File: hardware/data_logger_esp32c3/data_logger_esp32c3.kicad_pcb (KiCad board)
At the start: 4 copper layers, 43.3 x 32.3 mm, 74 parts, among them U1 ESP32-C3-MINI-1, U10 A03401A, U11 SX1509BIULTRT, U2 AZ1117IH-3.3TRG1, U4 LM321MF, U5 LM321MF, U6 LM321MF, U7 LM321MF, U8 LM321MF, U9 A03401A

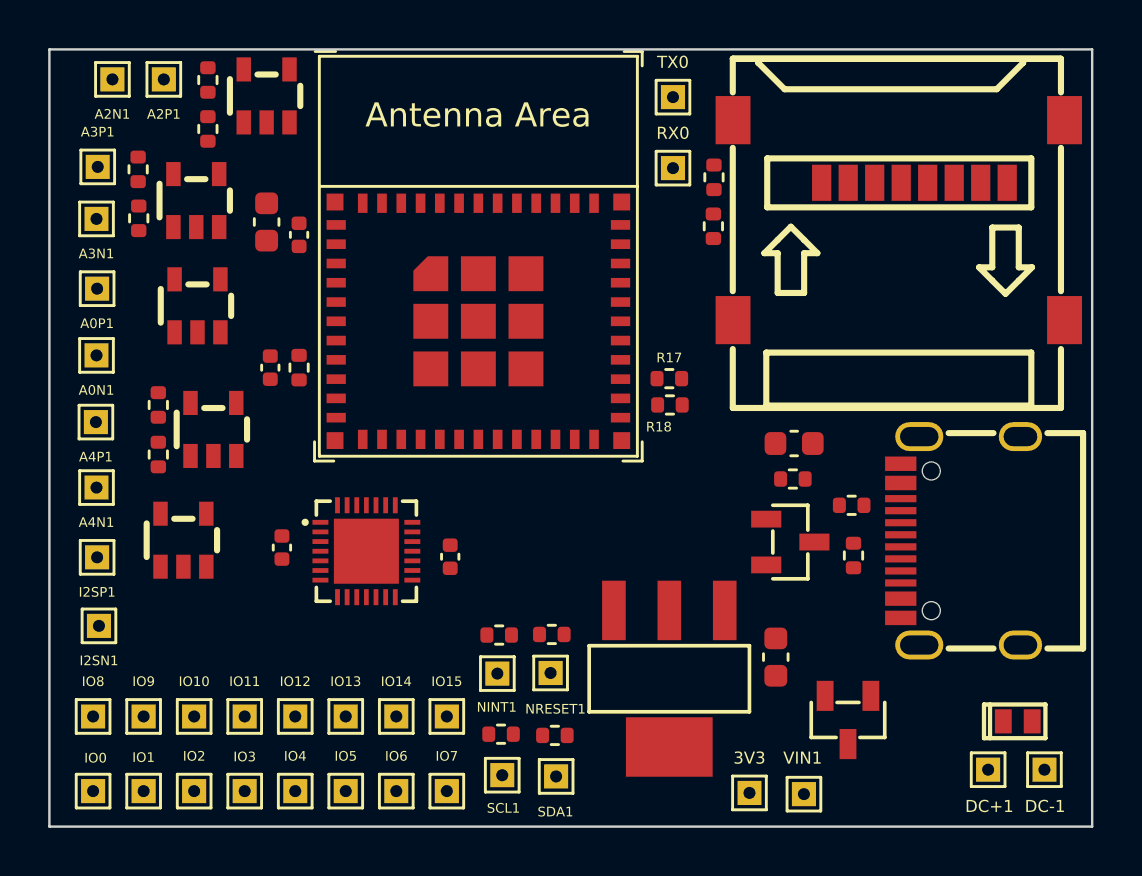
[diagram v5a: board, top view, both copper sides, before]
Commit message: added copper fills
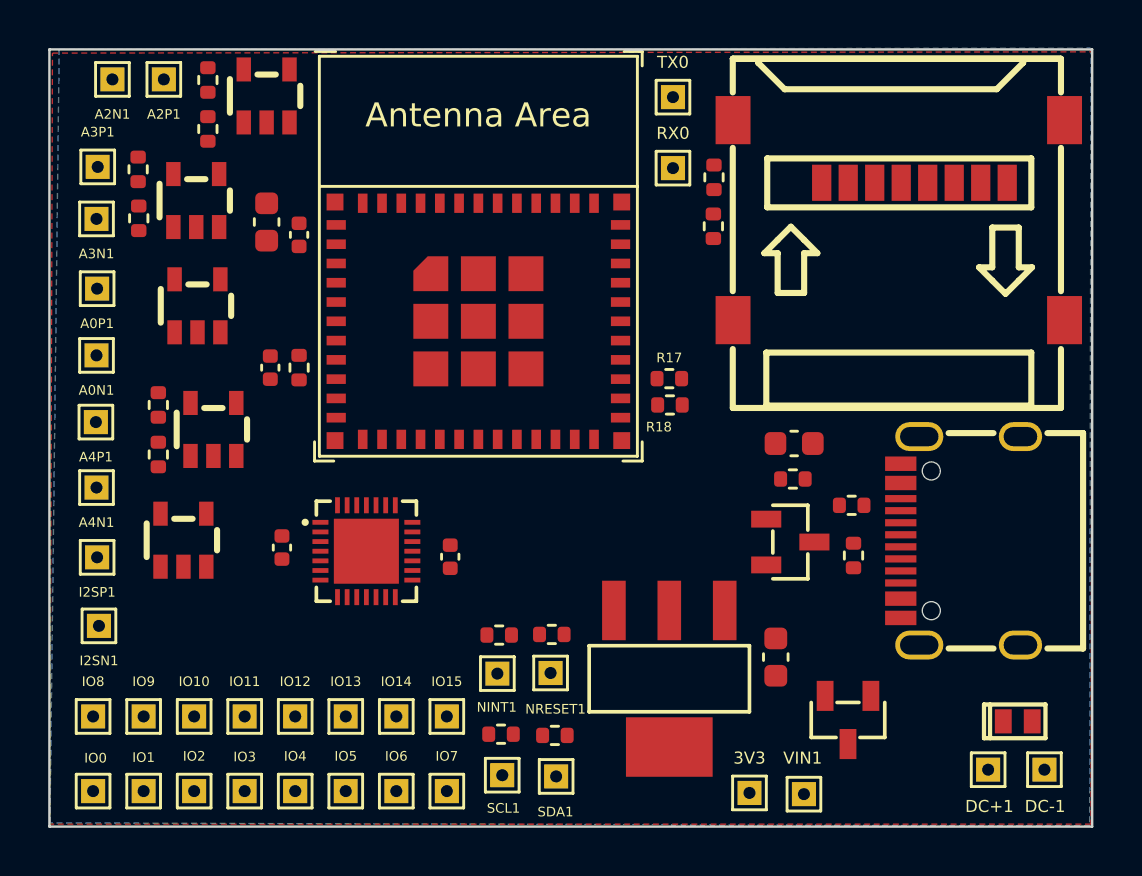
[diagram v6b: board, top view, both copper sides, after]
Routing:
- added copper zone on B.Cu, net GND
- added copper zone on F.Cu, net GND
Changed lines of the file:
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@@
   )
   (gr_rect (start 98.8568 49.6062) (end 142.1384 81.8642) (layer "Edge.Cuts") (width 0.1) (fill none))
+  (zone (net 2) (net_name "GND") (layer "F.Cu") (hatch edge 0.508)
+    (connect_pads (clearance 0.508))
+    (min_thickness 0.254) (filled_areas_thickness no)
+    (fill yes (thermal_gap 0.508) (thermal_bridge_width 0.508))
+    (polygon
+      (pts
+        (xy 142.0876 81.7626)
+        (xy 98.8822 81.7626)
+        (xy 98.9838 49.7586)
+        (xy 142.1384 49.7078)
+      )
+    )
+  )
   (zone (net 3) (net_name "+3V3") (layer "In1.Cu") (hatch edge 0.508)
     (connect_pads (clearance 0.508))
-    (min_thickness 0.254)
-    (fill (thermal_gap 0.508) (thermal_bridge_width 0.508))
+    (min_thickness 0.254) (filled_areas_thickness no)
+    (fill yes (thermal_gap 0.508) (thermal_bridge_width 0.508))
     (polygon
       (pts
@@
   (zone (net 2) (net_name "GND") (layer "In2.Cu") (hatch edge 0.508)
     (connect_pads (clearance 0.508))
-    (min_thickness 0.254)
-    (fill (thermal_gap 0.508) (thermal_bridge_width 0.508))
+    (min_thickness 0.254) (filled_areas_thickness no)
+    (fill yes (thermal_gap 0.508) (thermal_bridge_width 0.508))
     (polygon
       (pts
@@
       )
     )
+  )
+  (zone (net 2) (net_name "GND") (layer "B.Cu") (hatch edge 0.508)
+    (connect_pads (clearance 0.508))
+    (min_thickness 0.254) (filled_areas_thickness no)
+    (fill yes (thermal_gap 0.508) (thermal_bridge_width 0.508))
+    (polygon
+      (pts
+        (xy 142.0368 81.8388)
+        (xy 98.8822 81.7118)
+        (xy 99.2632 49.6062)
+        (xy 142.0876 49.5554)
+      )
+    )

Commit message: routing done
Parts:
- moved C4 5.29 mm to (125.6, 69.2), turned to 90 degrees
- moved R9 3.52 mm to (127.0, 69.7), turned to -90 degrees
- moved R7 1.43 mm to (132.0, 67.1)
- moved R2 0.52 mm to (131.9, 71.0)
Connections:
- net Net-(USB-C1-PadA6) renamed D_CONN+
- net Net-(USB-C1-PadA7) renamed D_CONN-
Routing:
- net +3V3: track 0.00 -> 26.7 mm, vias 0 -> 1
- net Net-(C4-Pad1): track 0.00 -> 20.4 mm
- net D_CONN+: track 0.00 -> 15.4 mm
- net D_CONN-: track 0.00 -> 15.1 mm
- net Net-(R3-Pad1): track 0.00 -> 13.7 mm
- net Net-(TX0-Pad1): track 0.00 -> 10.1 mm
- net Net-(D1-Pad1): track 0.00 -> 8.52 mm
- net Net-(RX0-Pad1): track 0.00 -> 7.99 mm
- net +5V: track 0.00 -> 6.35 mm
- net Net-(R1-Pad1): track 0.00 -> 5.45 mm
- net Net-(A0P1-Pad1): track 0.00 -> 3.97 mm
- net Net-(A4P1-Pad1): track 0.00 -> 3.10 mm
- net Net-(C1-Pad1): track 0.00 -> 2.83 mm
- net Net-(R11-Pad2): track 0.00 -> 2.82 mm
- net Net-(I2SP1-Pad1): track 0.00 -> 2.79 mm
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
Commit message: more layout
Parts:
- moved R7 1.06 mm to (132.7, 66.3), turned to -90 degrees
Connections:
- U1 pad 13: I2C_SDA -> I2C_SCL
- U1 pad 16: I2C_SCL -> I2C_SDA
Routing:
- net DO: track 0.00 -> 22.9 mm, vias 0 -> 2
- net SCLK: track 0.00 -> 20.6 mm, vias 0 -> 2
- net DI: track 0.00 -> 19.7 mm, vias 0 -> 2
- net CS: track 0.00 -> 19.5 mm, vias 0 -> 2
- net +3V3: track 26.7 -> 44.8 mm, vias 1 -> 16
- net I2S: track 2.20 -> 16.1 mm, vias 0 -> 2
- net ADC1_CH4: track 2.20 -> 13.2 mm, vias 0 -> 2
- net GND: track 0.00 -> 10.7 mm, vias 0 -> 18
- net ADC1_CH0: track 0.00 -> 10.4 mm, vias 0 -> 2
- net ADC1_CH2: track 2.20 -> 11.9 mm, vias 0 -> 2
- net ADC1_CH3: track 2.20 -> 9.26 mm
- net +5V: track 6.35 -> 13.1 mm
- net I2C_SDA: track 1.89 -> 6.19 mm
- net I2C_SCL: track 1.89 -> 4.90 mm
- net Net-(R2-Pad2): track 0.00 -> 2.41 mm
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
